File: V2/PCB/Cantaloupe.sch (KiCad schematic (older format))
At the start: 121 parts, among them J1 USB_In, J2 OLED, J3 Link, J4 Debug, J5 Trackball, Q1 2N7002, Q2 AO3401A, SW1 MX, SW10 MX, SW11 MX, SW12 MX, SW13 MX, SW14 MX, SW15 MX, SW16 MX, SW17 MX, SW18 MX, SW19 MX, SW2 MX, SW20 MX, SW21 MX, SW22 MX, SW23 MX, SW24 MX, SW25 MX, SW26 MX, SW27 MX, SW28 MX, SW29 MX, SW3 MX, SW30 MX, SW31 Encoder, SW32 MX, SW4 MX, SW5 MX, SW6 MX, SW7 MX, SW8 MX, SW9 MX, U1 STM32F4x1CxUx, U2 SRV0504, U3 SRV0504, U4 XC6206P332MR, U5 LMV321, Y1 8MHz

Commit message: Clean up of design. Added gerbers and files for FR4 plates.
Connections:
- net VBUS_In: no longer U2.5 (VP)
- net VBUS_Fused: now reaches F2.1, Q2.3 (D), R13.1, U5.3 (-)
- net VBUS_Fused: now also U2.5 (VP)
- net SWOCLK renamed SWCLK
- net SWOIO renamed SWDIO
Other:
- moved on the sheet: F1, F2, Q2, R13, R14, U5
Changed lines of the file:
@@
 Wire Notes Line
 	2100 5800 6400 5800
-Text GLabel 6900 4900 0    50   Input ~ 0
+Text GLabel 6900 6400 0    50   Input ~ 0
 VBUS_In
 $Comp
 L Device:Polyfuse_Small F1
 U 1 1 6233E288
-P 7000 4900
-F 0 "F1" V 6795 4900 50  0000 C CNN
-F 1 "500mA" V 6886 4900 50  0000 C CNN
-F 2 "Fuse:Fuse_1206_3216Metric" H 7050 4700 50  0001 L CNN
-F 3 "~" H 7000 4900 50  0001 C CNN
-	1    7000 4900
+P 7000 6400
+F 0 "F1" V 6795 6400 50  0000 C CNN
+F 1 "500mA" V 6886 6400 50  0000 C CNN
+F 2 "Fuse:Fuse_1206_3216Metric" H 7050 6200 50  0001 L CNN
+F 3 "~" H 7000 6400 50  0001 C CNN
+	1    7000 6400
 	0    1    1    0
 $EndComp
-Text GLabel 7100 4900 2    50   Input ~ 0
+Text GLabel 7100 6400 2    50   Input ~ 0
 VBUS_In_Fused
 Text GLabel 9200 800  2    50   Input ~ 0
@@
 	4400 1000 4800 1000
 Text GLabel 5600 3700 2    50   Input ~ 0
-SWOIO
+SWDIO
 $Comp
 L MCU_ST_STM32F4:STM32F411CCUx U1
@@
 	10100 5200 10000 5200
 Text GLabel 5600 3800 2    50   Input ~ 0
-SWOCLK
+SWCLK
 NoConn ~ 5600 3900
 NoConn ~ 4300 2800
-Text GLabel 5800 5100 0    50   Input ~ 0
-SWOIO
-Text GLabel 5800 5200 0    50   Input ~ 0
-SWOCLK
 Wire Notes Line
 	6400 4600 5400 4600
@@
 NoConn ~ 9000 3600
 Text GLabel 7000 3200 0    50   Input ~ 0
-VBUS_In
+VBUS_Fused
 Connection ~ 8500 3200
 Wire Wire Line
@@
 Wire Notes Line
 	8500 6500 8500 4600
-Text GLabel 8400 5200 1    50   Input ~ 0
+Text GLabel 8400 5000 1    50   Input ~ 0
 VBUS_In
 Wire Wire Line
-	7700 5700 7700 5600
+	7700 5500 7700 5400
 $Comp
 L Transistor_FET:AO3401A Q2
 U 1 1 62437866
-P 7700 5400
-F 0 "Q2" V 8042 5400 50  0000 C CNN
-F 1 "AO3401A" V 7951 5400 50  0000 C CNN
-F 2 "Package_TO_SOT_SMD:SOT-23" H 7900 5325 50  0001 L CIN
-F 3 "http://www.aosmd.com/pdfs/datasheet/AO3401A.pdf" H 7700 5400 50  0001 L CNN
-	1    7700 5400
+P 7700 5200
+F 0 "Q2" V 8042 5200 50  0000 C CNN
+F 1 "AO3401A" V 7951 5200 50  0000 C CNN
+F 2 "Package_TO_SOT_SMD:SOT-23" H 7900 5125 50  0001 L CIN
+F 3 "http://www.aosmd.com/pdfs/datasheet/AO3401A.pdf" H 7700 5200 50  0001 L CNN
+	1    7700 5200
 	0    -1   -1   0
 $EndComp
 Wire Wire Line
-	7800 5700 7700 5700
-Wire Wire Line
-	7500 6100 8400 6100
+	7800 5500 7700 5500
+Wire Wire Line
+	7500 5900 8400 5900
 $Comp
 L power:GND #PWR0123
 U 1 1 631C4FB0
-P 8200 6200
-F 0 "#PWR0123" H 8200 5950 50  0001 C CNN
-F 1 "GND" H 8205 6027 50  0000 C CNN
-F 2 "" H 8200 6200 50  0001 C CNN
-F 3 "" H 8200 6200 50  0001 C CNN
-	1    8200 6200
-	1    0    0    -1
-$EndComp
-Wire Wire Line
-	8400 5200 8400 5300
-Connection ~ 8400 5300
-Wire Wire Line
-	8400 5800 8400 6100
-Wire Wire Line
-	8400 5600 8400 5300
-Wire Wire Line
-	7900 5300 8200 5300
-Connection ~ 8200 5300
-Wire Wire Line
-	8200 5300 8400 5300
-Wire Wire Line
-	8200 5400 8200 5300
-Wire Wire Line
-	8200 6000 8200 6200
-Wire Wire Line
-	7500 5300 7500 6100
+P 8200 6000
+F 0 "#PWR0123" H 8200 5750 50  0001 C CNN
+F 1 "GND" H 8205 5827 50  0000 C CNN
+F 2 "" H 8200 6000 50  0001 C CNN
+F 3 "" H 8200 6000 50  0001 C CNN
+	1    8200 6000
+	1    0    0    -1
+$EndComp
+Wire Wire Line
+	8400 5000 8400 5100
+Connection ~ 8400 5100
+Wire Wire Line
+	8400 5600 8400 5900
+Wire Wire Line
+	8400 5400 8400 5100
+Wire Wire Line
+	7900 5100 8200 5100
+Connection ~ 8200 5100
+Wire Wire Line
+	8200 5100 8400 5100
+Wire Wire Line
+	8200 5200 8200 5100
+Wire Wire Line
+	8200 5800 8200 6000
+Wire Wire Line
+	7500 5100 7500 5900
 $Comp
 L Amplifier_Operational:LMV321 U5
 U 1 1 62452FE5
-P 8100 5700
-F 0 "U5" H 8200 6000 50  0000 C CNN
-F 1 "LMV321" H 8200 5900 50  0000 C CNN
-F 2 "Package_TO_SOT_SMD:SOT-23-5" H 8100 5700 50  0001 L CNN
-F 3 "http://www.ti.com/lit/ds/symlink/lmv324.pdf" H 8100 5700 50  0001 C CNN
-	1    8100 5700
+P 8100 5500
+F 0 "U5" H 8200 5800 50  0000 C CNN
+F 1 "LMV321" H 8200 5700 50  0000 C CNN
+F 2 "Package_TO_SOT_SMD:SOT-23-5" H 8100 5500 50  0001 L CNN
+F 3 "http://www.ti.com/lit/ds/symlink/lmv324.pdf" H 8100 5500 50  0001 C CNN
+	1    8100 5500
 	-1   0    0    -1
 $EndComp
@@
 L Device:Polyfuse_Small F2
 U 1 1 6240F7C8
-P 7000 5300
-F 0 "F2" V 6795 5300 50  0000 C CNN
-F 1 "1A" V 6886 5300 50  0000 C CNN
-F 2 "Fuse:Fuse_1206_3216Metric" H 7050 5100 50  0001 L CNN
-F 3 "~" H 7000 5300 50  0001 C CNN
-	1    7000 5300
+P 7000 5100
+F 0 "F2" V 6795 5100 50  0000 C CNN
+F 1 "1A" V 6886 5100 50  0000 C CNN
+F 2 "Fuse:Fuse_1206_3216Metric" H 7050 4900 50  0001 L CNN
+F 3 "~" H 7000 5100 50  0001 C CNN
+	1    7000 5100
 	0    1    1    0
 $EndComp
 Wire Wire Line
-	6900 5300 6800 5300
-Text GLabel 6800 5300 0    50   Input ~ 0
+	6900 5100 6800 5100
+Text GLabel 6800 5100 0    50   Input ~ 0
 VBUS
-Connection ~ 7500 5300
-Wire Wire Line
-	7200 5300 7500 5300
-Wire Wire Line
-	7200 5300 7100 5300
-Connection ~ 7200 5300
-Wire Wire Line
-	7200 5400 7200 5300
+Connection ~ 7500 5100
+Wire Wire Line
+	7200 5100 7500 5100
+Wire Wire Line
+	7200 5100 7100 5100
+Connection ~ 7200 5100
+Wire Wire Line
+	7200 5200 7200 5100
 $Comp
 L power:GND #PWR0138
 U 1 1 62427BC2
-P 7200 6000
-F 0 "#PWR0138" H 7200 5750 50  0001 C CNN
-F 1 "GND" H 7205 5827 50  0000 C CNN
-F 2 "" H 7200 6000 50  0001 C CNN
-F 3 "" H 7200 6000 50  0001 C CNN
-	1    7200 6000
+P 7200 5800
+F 0 "#PWR0138" H 7200 5550 50  0001 C CNN
+F 1 "GND" H 7205 5627 50  0000 C CNN
+F 2 "" H 7200 5800 50  0001 C CNN
+F 3 "" H 7200 5800 50  0001 C CNN
+	1    7200 5800
 	1    0    0    -1
 $EndComp
@@
 L Device:R_Small R14
 U 1 1 6250C728
-P 7200 5900
-F 0 "R14" H 7259 5946 50  0000 L CNN
-F 1 "200k" H 7259 5855 50  0000 L CNN
-F 2 "Resistor_SMD:R_0603_1608Metric" H 7200 5900 50  0001 C CNN
-F 3 "~" H 7200 5900 50  0001 C CNN
-	1    7200 5900
-	1    0    0    -1
-$EndComp
-Wire Wire Line
-	7200 5800 7200 5700
-Wire Wire Line
-	7200 5700 7200 5600
-Connection ~ 7200 5700
-Wire Wire Line
-	7100 5700 7200 5700
-Text GLabel 7100 5700 0    50   Input ~ 0
+P 7200 5700
+F 0 "R14" H 7259 5746 50  0000 L CNN
+F 1 "200k" H 7259 5655 50  0000 L CNN
+F 2 "Resistor_SMD:R_0603_1608Metric" H 7200 5700 50  0001 C CNN
+F 3 "~" H 7200 5700 50  0001 C CNN
+	1    7200 5700
+	1    0    0    -1
+$EndComp
+Wire Wire Line
+	7200 5600 7200 5500
+Wire Wire Line
+	7200 5500 7200 5400
+Connection ~ 7200 5500
+Wire Wire Line
+	7100 5500 7200 5500
+Text GLabel 7100 5500 0    50   Input ~ 0
 PLUGGED
 $Comp
 L Device:R_Small R13
 U 1 1 624179D2
-P 7200 5500
-F 0 "R13" H 7259 5546 50  0000 L CNN
-F 1 "100k" H 7259 5455 50  0000 L CNN
-F 2 "Resistor_SMD:R_0603_1608Metric" H 7200 5500 50  0001 C CNN
-F 3 "~" H 7200 5500 50  0001 C CNN
-	1    7200 5500
+P 7200 5300
+F 0 "R13" H 7259 5346 50  0000 L CNN
+F 1 "100k" H 7259 5255 50  0000 L CNN
+F 2 "Resistor_SMD:R_0603_1608Metric" H 7200 5300 50  0001 C CNN
+F 3 "~" H 7200 5300 50  0001 C CNN
+	1    7200 5300
 	1    0    0    -1
 $EndComp
 Text GLabel 5600 3200 2    50   Input ~ 0
 PLUGGED
+Text GLabel 7100 4800 0    50   Input ~ 0
+VBUS_Fused
+Wire Wire Line
+	7200 5100 7200 4800
+Wire Wire Line
+	7200 4800 7100 4800
+Text GLabel 5800 5100 0    50   Input ~ 0
+SWDIO
+Text GLabel 5800 5200 0    50   Input ~ 0
+SWCLK
 $EndSCHEMATC

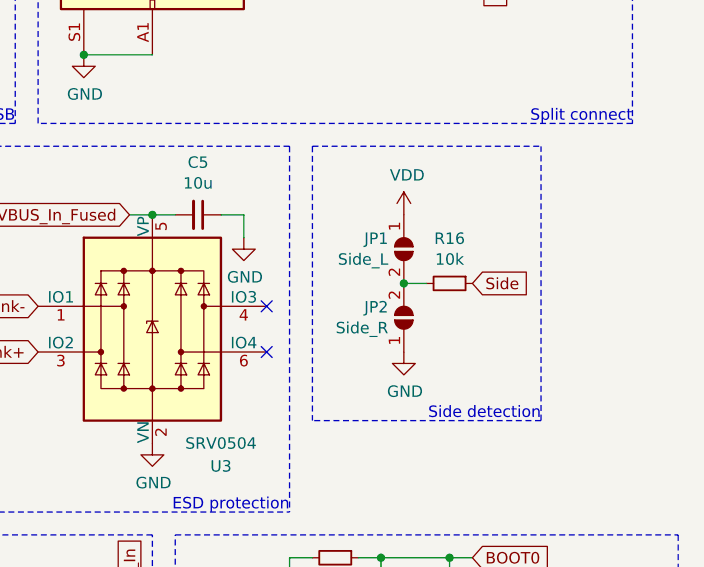
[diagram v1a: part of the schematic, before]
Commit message: Fixed jumper side
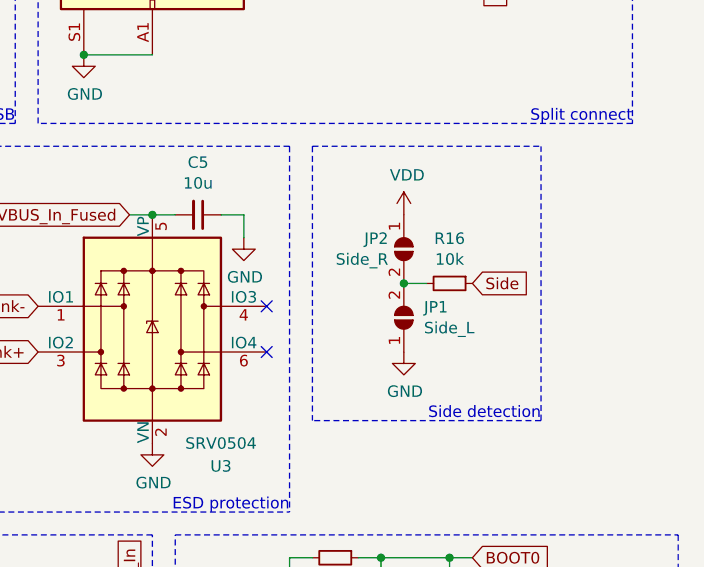
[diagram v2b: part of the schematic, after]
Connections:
- net GND: now also JP1.1 (A); no longer JP2.1 (A)
- net VDD: now also JP2.1 (A); no longer JP1.1 (A)
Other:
- moved on the sheet: JP1, JP2
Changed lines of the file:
@@
 L Jumper:SolderJumper_2_Open JP2
 U 1 1 6217ADB0
+P 9600 3350
+F 0 "JP2" V 9554 3418 50  0000 L CNN
+F 1 "Side_R" V 9645 3418 50  0000 L CNN
+F 2 "Jumper:SolderJumper-2_P1.3mm_Open_Pad1.0x1.5mm" H 9600 3350 50  0001 C CNN
+F 3 "~" H 9600 3350 50  0001 C CNN
+	1    9600 3350
+	0    -1   1    0
+$EndComp
+$Comp
+L Jumper:SolderJumper_2_Open JP1
+U 1 1 6217ADB6
 P 9600 3650
-F 0 "JP2" V 9646 3718 50  0000 L CNN
-F 1 "Side_R" V 9555 3718 50  0000 L CNN
+F 0 "JP1" V 9646 3562 50  0000 R CNN
+F 1 "Side_L" V 9555 3562 50  0000 R CNN
 F 2 "Jumper:SolderJumper-2_P1.3mm_Open_Pad1.0x1.5mm" H 9600 3650 50  0001 C CNN
 F 3 "~" H 9600 3650 50  0001 C CNN
@@
 	0    -1   -1   0
 $EndComp
-$Comp
-L Jumper:SolderJumper_2_Open JP1
-U 1 1 6217ADB6
-P 9600 3350
-F 0 "JP1" V 9554 3418 50  0000 L CNN
-F 1 "Side_L" V 9645 3418 50  0000 L CNN
-F 2 "Jumper:SolderJumper-2_P1.3mm_Open_Pad1.0x1.5mm" H 9600 3350 50  0001 C CNN
-F 3 "~" H 9600 3350 50  0001 C CNN
-	1    9600 3350
-	0    -1   1    0
-$EndComp
 Wire Wire Line
 	9700 3500 9600 3500
-Connection ~ 9600 3500
 $Comp
 L power:VDD #PWR0127
@@
 Text GLabel 5800 5200 0    50   Input ~ 0
 SWCLK
+Connection ~ 9600 3500
 $EndSCHEMATC
